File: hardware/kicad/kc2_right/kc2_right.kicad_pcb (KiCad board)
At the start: 2 copper layers, 194.8 x 133.8 mm, 96 parts, among them SW1 KEY_01, SW10 KEY_10, SW11 KEY_11, SW12 KEY_12, SW13 KEY_13, SW14 KEY_14, SW15 KEY_15, SW16 KEY_16, SW17 KEY_17, SW18 KEY_18, SW19 KEY_19, SW2 KEY_02, SW20 KEY_20, SW21 KEY_21, SW22 KEY_22, SW23 KEY_23, SW24 KEY_24, SW25 KEY_25, SW26 KEY_26, SW27 KEY_27, SW28 KEY_28, SW29 KEY_29, SW3 KEY_03, SW30 KEY_30, SW31 KEY_31, SW32 KEY_32, SW33 KEY_33, SW34 KEY_34, SW35 KEY_35, SW36 KEY_36, SW37 KEY_37, SW38 KEY_38, SW39 KEY_39, SW4 KEY_04, SW40 KEY_40, SW41 KEY_41, SW42 KEY_42, SW43 KEY_43, SW44 KEY_44, SW45 KEY_45, SW5 KEY_05, SW6 KEY_06, SW7 KEY_07, SW8 KEY_08, SW9 KEY_09, U1 nice!nano_v2_socket_24pin

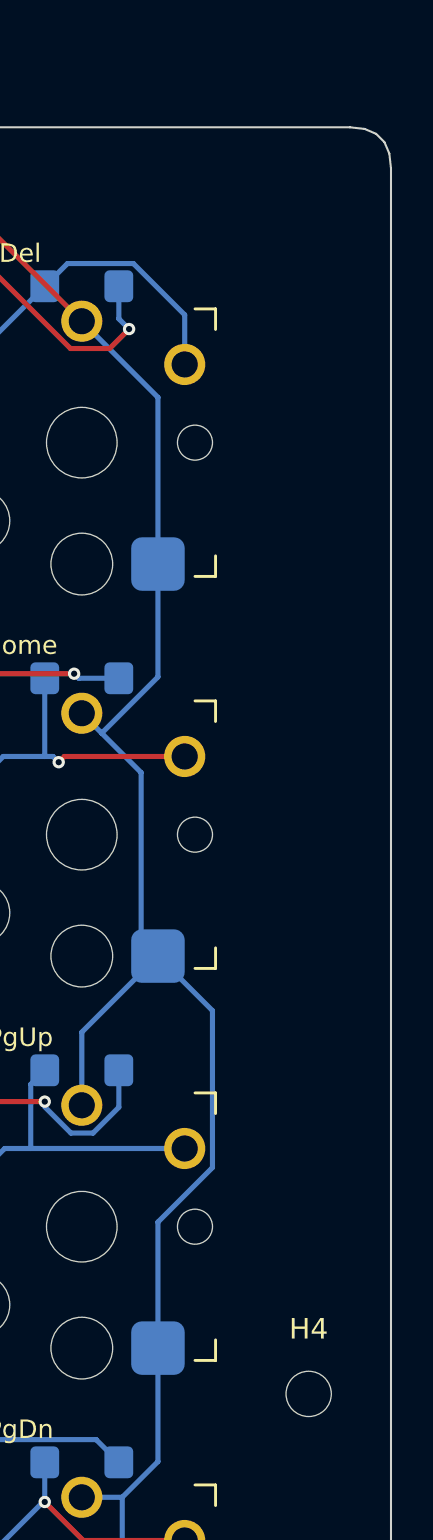
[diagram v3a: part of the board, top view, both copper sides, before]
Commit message: fix: KC2 X3 H4/H5 마운팅 홀 배치 조정
H4를 한 줄 위로 옮기고 H2 인접 상단 코너에 H5를 추가해 하부 바닥판 고정 지점 분포를 개선
왼쪽은 상단 외곽 제약 때문에 H2.x보다 안쪽인 x=173.45에 H5를 배치
관련 산출물과 검증 증거를 동일 보드 상태로 재생성
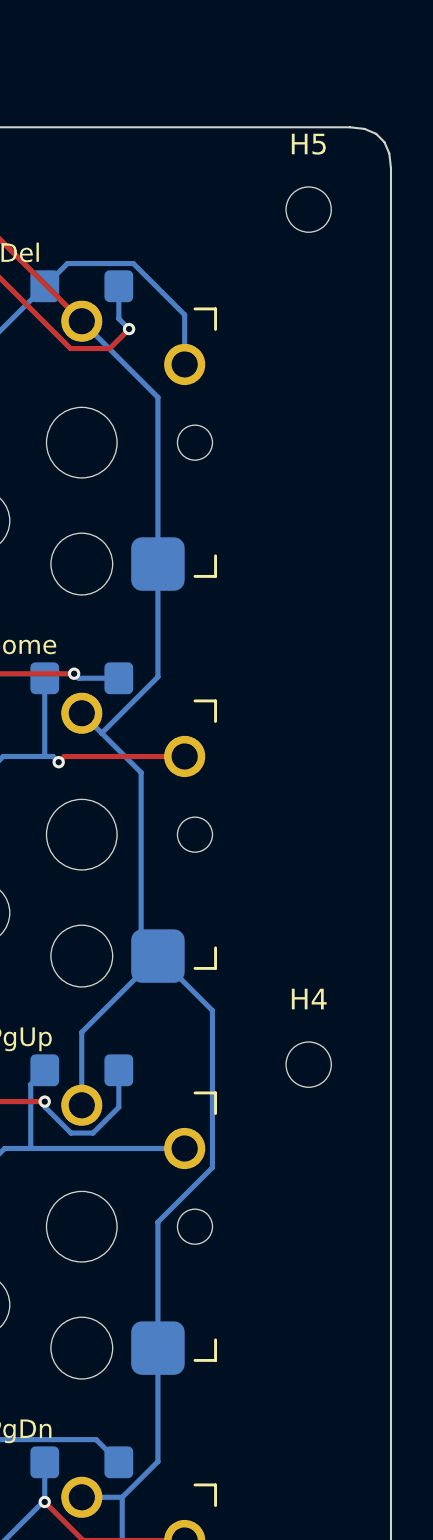
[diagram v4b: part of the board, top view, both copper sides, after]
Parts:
- added H5: M2_NPTH_2.2, MountingHole_2.2mm_M2, F.Cu at (225.8, 66.2)
- moved H4 16.0 mm to (225.8, 107.8)
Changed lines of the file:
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@@
 		(embedded_fonts no)
 	)
+	(footprint "MountingHole_2.2mm_M2"
+		(layer "F.Cu")
+		(at 225.8375 66.2)
+		(descr "Mounting Hole 2.2mm, M2, no annular, generated by kicad-footprint-generator mountinghole.py")
+		(tags "mountinghole M2")
+		(property "Reference" "H5"
+			(at 0 -3.15 0)
+			(layer "F.SilkS")
+			(effects
+				(font
+					(size 1 1)
+					(thickness 0.15)
+				)
+			)
+		)
+		(property "Value" "M2_NPTH_2.2"
+			(at 0 3.15 0)
+			(layer "F.Fab")
+			(effects
+				(font
+					(size 1 1)
+					(thickness 0.15)
+				)
+			)
+		)
+		(property "Datasheet" ""
+			(at 0 0 0)
+			(layer "F.Fab")
+			(hide yes)
+			(effects
+				(font
+					(size 1.27 1.27)
+				)
+			)
+		)
+		(property "Description" ""
+			(at 0 0 0)
+			(layer "F.Fab")
+			(hide yes)
+			(effects
+				(font
+					(size 1.27 1.27)
+				)
+			)
+		)
+		(property "KiLib_Generator" "mounting_hardware/mounting_hole"
+			(at 0 0 0)
+			(layer "F.SilkS")
+			(hide yes)
+			(effects
+				(font
+					(size 1 1)
+					(thickness 0.15)
+				)
+			)
+		)
+		(attr exclude_from_pos_files exclude_from_bom)
+		(duplicate_pad_numbers_are_jumpers no)
+		(fp_circle
+			(center 0 0)
+			(end 2.2 0)
+			(stroke
+				(width 0.15)
+				(type solid)
+			)
+			(fill no)
+			(layer "Cmts.User")
+		)
+		(fp_circle
+			(center 0 0)
+			(end 2.45 0)
+			(stroke
+				(width 0.05)
+				(type solid)
+			)
+			(fill no)
+			(layer "F.CrtYd")
+		)
+		(fp_text user "${REFERENCE}"
+			(at 0 0 0)
+			(layer "F.Fab")
+			(effects
+				(font
+					(size 1 1)
+					(thickness 0.15)
+				)
+			)
+		)
+		(pad "" np_thru_hole circle
+			(at 0 0)
+			(size 2.2 2.2)
+			(drill 2.2)
+			(layers "*.Cu" "*.Mask")
+		)
+		(embedded_fonts no)
+	)
 	(footprint "SW_Kailh_Choc_V1_HotSwap_THT"
 		(layer "F.Cu")
@@
 	(footprint "MountingHole_2.2mm_M2"
 		(layer "F.Cu")
-		(at 225.8375 123.75)
+		(at 225.8375 107.75)
 		(descr "Mounting Hole 2.2mm, M2, no annular, generated by kicad-footprint-generator mountinghole.py")
 		(tags "mountinghole M2")
@@
 	)
 	(gr_line
-		(start 223.3375 121.25)
-		(end 228.3375 121.25)
+		(start 223.3375 63.7)
+		(end 228.3375 63.7)
+		(stroke
+			(width 0.08)
+			(type default)
+		)
+		(layer "Cmts.User")
+	)
+	(gr_line
+		(start 223.3375 68.7)
+		(end 223.3375 63.7)
+		(stroke
+			(width 0.08)
+			(type default)
+		)
+		(layer "Cmts.User")
+	)
+	(gr_line
+		(start 223.3375 105.25)
+		(end 228.3375 105.25)
 		(stroke
 			(width 0.08)
@@
 	)
 	(gr_line
-		(start 223.3375 126.25)
-		(end 223.3375 121.25)
+		(start 223.3375 110.25)
+		(end 223.3375 105.25)
 		(stroke
 			(width 0.08)
@@
 	)
 	(gr_line
-		(start 228.3375 121.25)
-		(end 228.3375 126.25)
+		(start 228.3375 63.7)
+		(end 228.3375 68.7)
+		(stroke
+			(width 0.08)
+			(type default)
+		)
+		(layer "Cmts.User")
+	)
+	(gr_line
+		(start 228.3375 68.7)
+		(end 223.3375 68.7)
+		(stroke
+			(width 0.08)
+			(type default)
+		)
+		(layer "Cmts.User")
+	)
+	(gr_line
+		(start 228.3375 105.25)
+		(end 228.3375 110.25)
 		(stroke
 			(width 0.08)
@@
 	)
 	(gr_line
-		(start 228.3375 126.25)
-		(end 223.3375 126.25)
+		(start 228.3375 110.25)
+		(end 223.3375 110.25)
 		(stroke
 			(width 0.08)

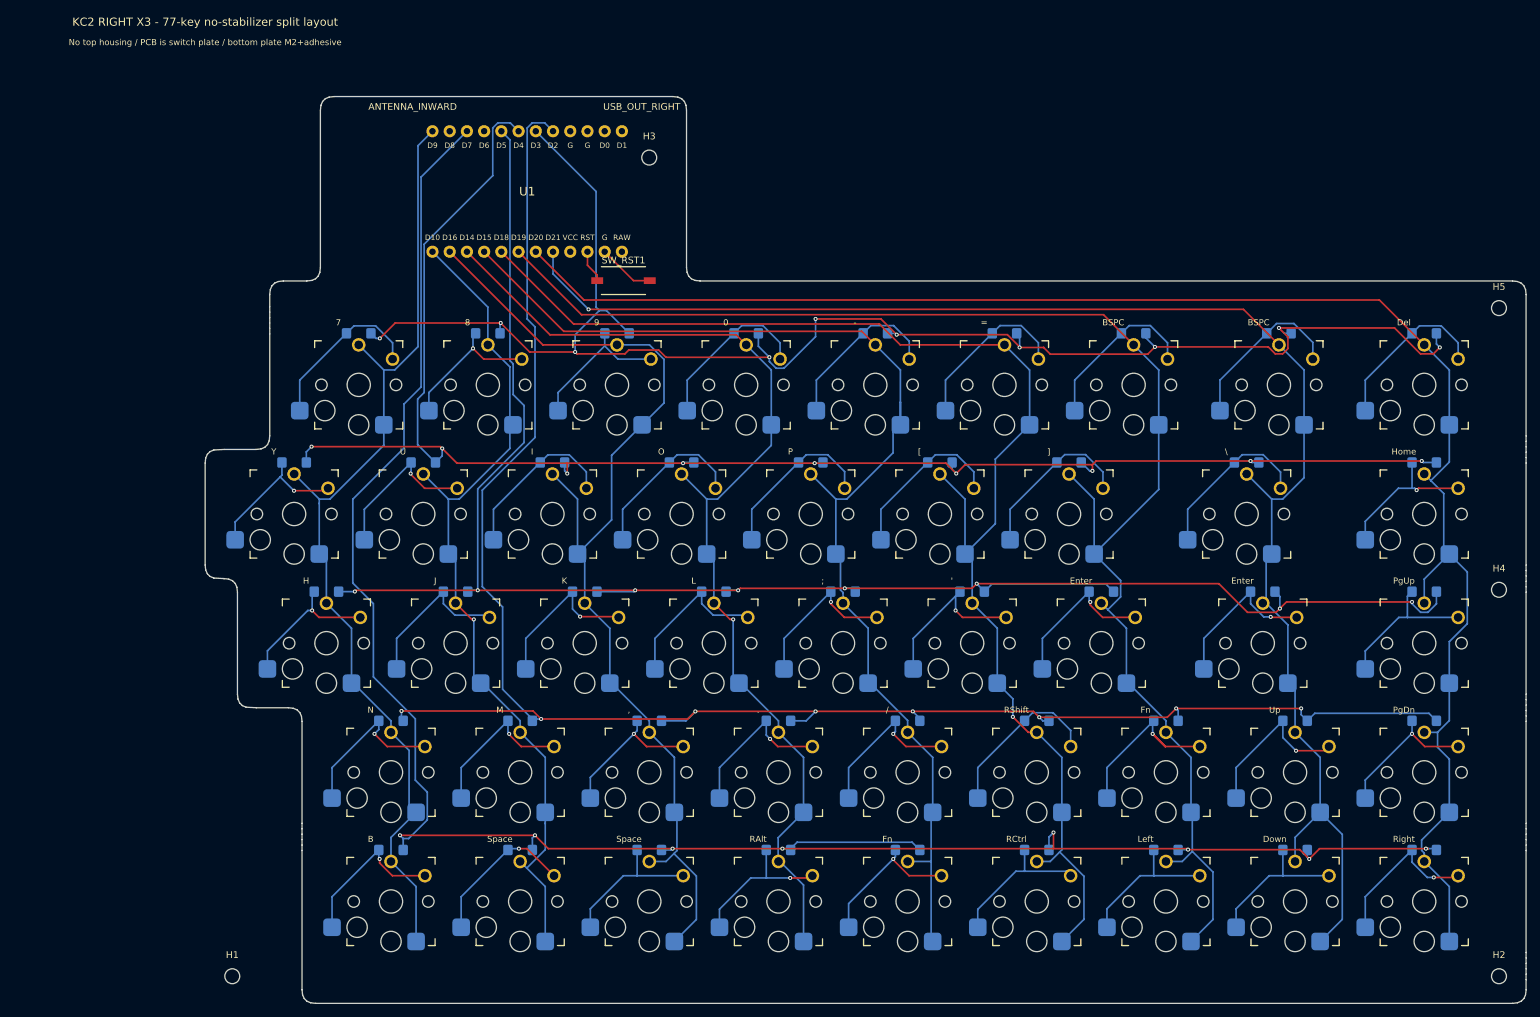
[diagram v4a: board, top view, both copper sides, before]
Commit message: feat: KC2 X3 스크류리스 주문 패키지를 주문 가능 상태로 갱신한다
스크류리스 레일 하우징용 주문 가능 상태를 확정하기 위해 M2 고정홀을 제거하고 REG_NPTH 등록홀, H1-H9 라벨, 배터리 리드 슬롯, antenna-side reset 위치, KC2 v1.0 L/R 실크를 반영한다.

DRC, 연결성, 실크 간섭, 키캡 간격, Gerber/drill/render/JLCPCB ZIP 검증기를 보강하고 주문 산출물을 재생성한다.

SpecKiwi 요구사항 증거와 Freerouting 프로세스 안전 규칙을 함께 갱신한다.
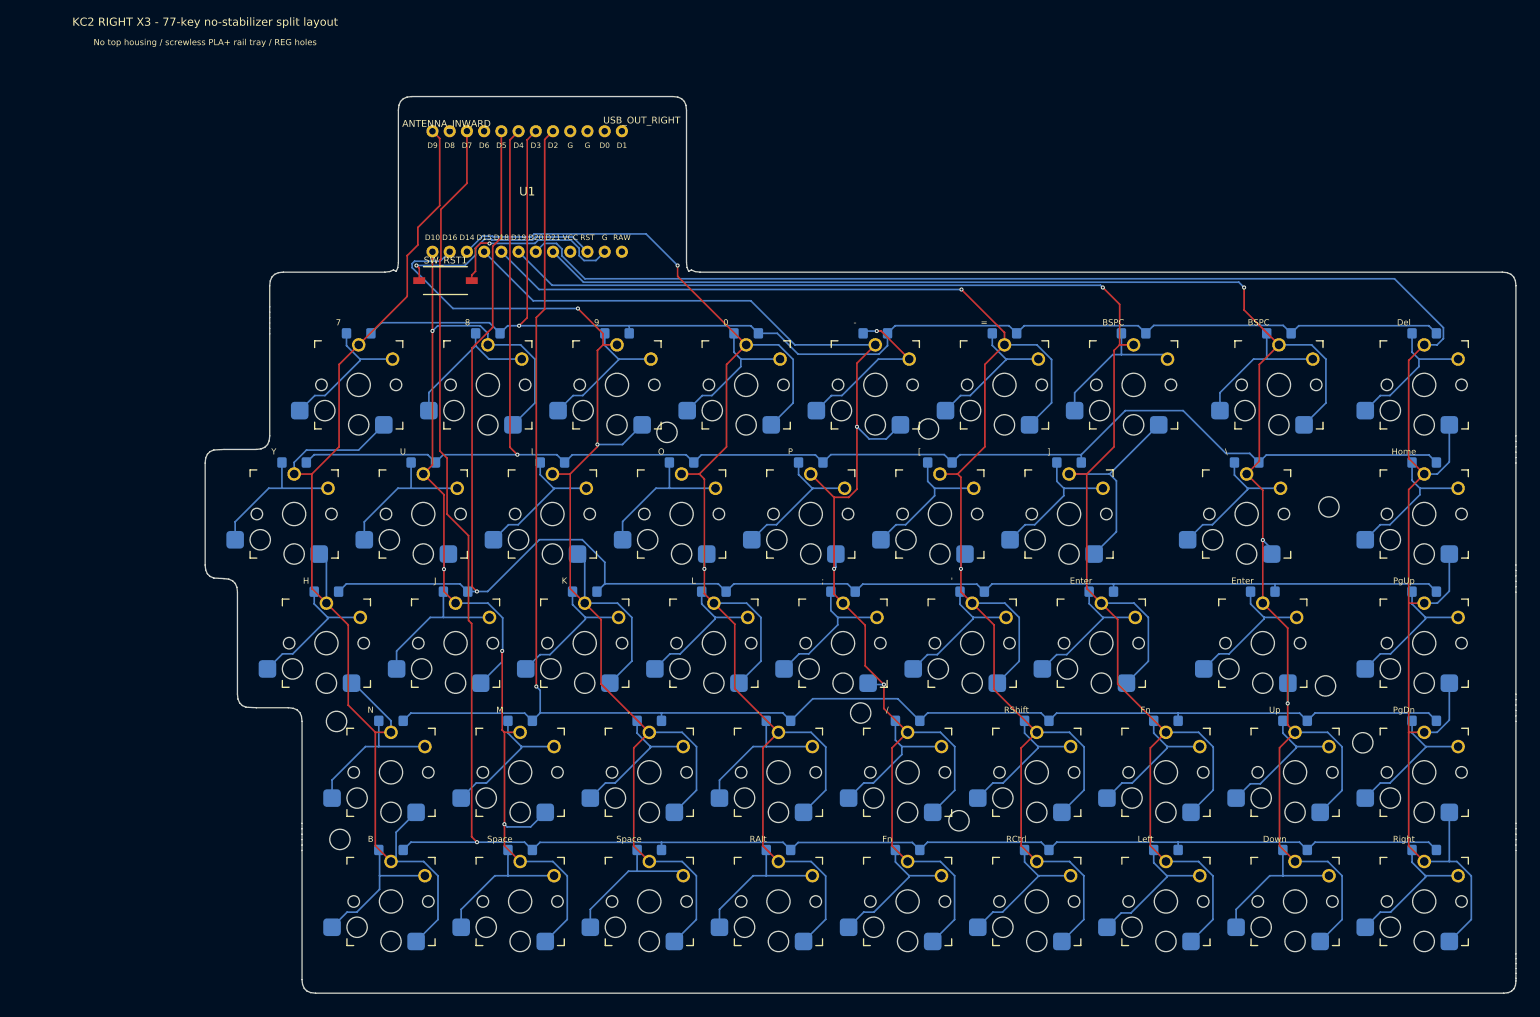
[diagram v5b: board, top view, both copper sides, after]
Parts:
- removed H1, H2, H3, H4, H5: M2_NPTH_2.2, MountingHole_2.2mm_M2
- added BAT_LEAD_SLOT1: BAT_LEAD_NPTH_SLOT_3.6x2.2, BAT_LEAD_NPTH_SLOT_3.6x2.2, F.Cu at (66.6, 49.0)
- added REG1: REG_NPTH_3.0, REG_NPTH_3.0, F.Cu at (103.1, 84.5)
- added REG2: REG_NPTH_3.0, REG_NPTH_3.0, F.Cu at (141.7, 84.0)
- added REG3: REG_NPTH_3.0, REG_NPTH_3.0, F.Cu at (200.8, 95.5)
- added REG4: REG_NPTH_3.0, REG_NPTH_3.0, F.Cu at (54.4, 127.2)
- added REG5: REG_NPTH_3.0, REG_NPTH_3.0, F.Cu at (131.7, 125.9)
- added REG6: REG_NPTH_3.0, REG_NPTH_3.0, F.Cu at (200.2, 121.9)
- added REG7: REG_NPTH_3.0, REG_NPTH_3.0, F.Cu at (54.9, 144.6)
- added REG8: REG_NPTH_3.0, REG_NPTH_3.0, F.Cu at (146.2, 141.8)
- added REG9: REG_NPTH_3.0, REG_NPTH_3.0, F.Cu at (205.8, 130.3)
- moved SW_RST1 26.2 mm to (70.5, 62.1)
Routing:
- net R_COL3: track 156.1 -> 216.2 mm, vias 1 -> 2
- net R_COL6: track 219.4 -> 273.8 mm, vias 0 -> 1
- net R_COL5: track 200.3 -> 247.2 mm, vias 1 -> 2
- net R_COL2: track 155.9 -> 202.4 mm, vias 0 -> 2
- net R_ROW4: track 310.1 -> 269.1 mm, vias 8 -> 1
- net R_ROW0: track 237.5 -> 197.6 mm, vias 10 -> 1
- net R_COL0: track 147.9 -> 187.8 mm
- net R_COL1: track 127.0 -> 165.6 mm, vias 1 -> 4
- net R_COL8: track 247.8 -> 285.3 mm
- net R_COL7: track 228.0 -> 259.8 mm, vias 1 -> 3
- net R_COL4: track 176.1 -> 205.1 mm, vias 0 -> 3
- net R_ROW2: track 275.1 -> 247.8 mm, vias 8 -> 1
- net RST: track 4.85 -> 31.2 mm, vias 0 -> 1
- net R_ROW3: track 273.6 -> 249.2 mm, vias 8 -> 1
- net GND: track 8.41 -> 27.0 mm, vias 0 -> 1
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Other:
- board size 194.8 x 133.8 mm -> 193.3 x 132.2 mm
- board text added: "BAT LEAD EXIT"
- board text added: "H1"
- board text added: "H2"
- board text added: "H3"
- board text added: "H4"
- board text added: "H5"
- board text added: "H6"
- board text added: "H7"
- board text added: "H8"
- board text added: "H9"
- board text added: "KC2 v1.0 R"
- board text added: "No top housing / screwless PLA+ rail tray / REG holes"
- board text removed: "No top housing / PCB is switch plate / bottom plate M2+adhesive"
